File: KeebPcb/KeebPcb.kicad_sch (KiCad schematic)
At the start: 0 parts

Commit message: MCU setup done
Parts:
- added C1: 1uF, symbol Device:C_Small
- added C2, C3, C4: 0.1uF, symbol Device:C_Small
- added C5: 10uF, symbol Device:C_Small
- added C6, C7: 22pF, symbol Device:C_Small
- added R1, R4: 10k, symbol Device:R_Small
- added R2, R3: 22, symbol Device:R_Small
- added SW1: SW_Push, symbol Switch:SW_Push
- added U1: ATmega32U4-A, Package_QFP:TQFP-44_10x10mm_P0.8mm, symbol MCU_Microchip_ATmega:ATmega32U4-A
- added Y1: 16MHz, symbol Device:Crystal_GND24_Small
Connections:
- new net: C1.1, U1.6 (UCAP)
- new net: R3.2, U1.3 (D-)
- new net: R4.2, SW1.2, U1.13 (~{RESET})
- new net: R2.2, U1.4 (D+)
- new net: R1.1, U1.33 (~{HWB}/PE2)
- new net: C6.2, U1.17 (XTAL1), Y1.1
- new net: C7.2, U1.16 (XTAL2), Y1.3
- new net +5V: C2.1, C3.1, C4.1, C5.1, R4.1, U1.14 (VCC), U1.2 (UVCC), U1.24 (AVCC), U1.34 (VCC), U1.44 (AVCC), U1.7 (VBUS)
- new net D+: R2.1
- new net D-: R3.1
- new net GND: C1.2, C2.2, C3.2, C4.2, C5.2, C6.1, C7.1, R1.2, SW1.1, U1.15 (GND), U1.23 (GND), U1.35 (GND), U1.43 (GND), U1.5 (UGND), Y1.2, Y1.4

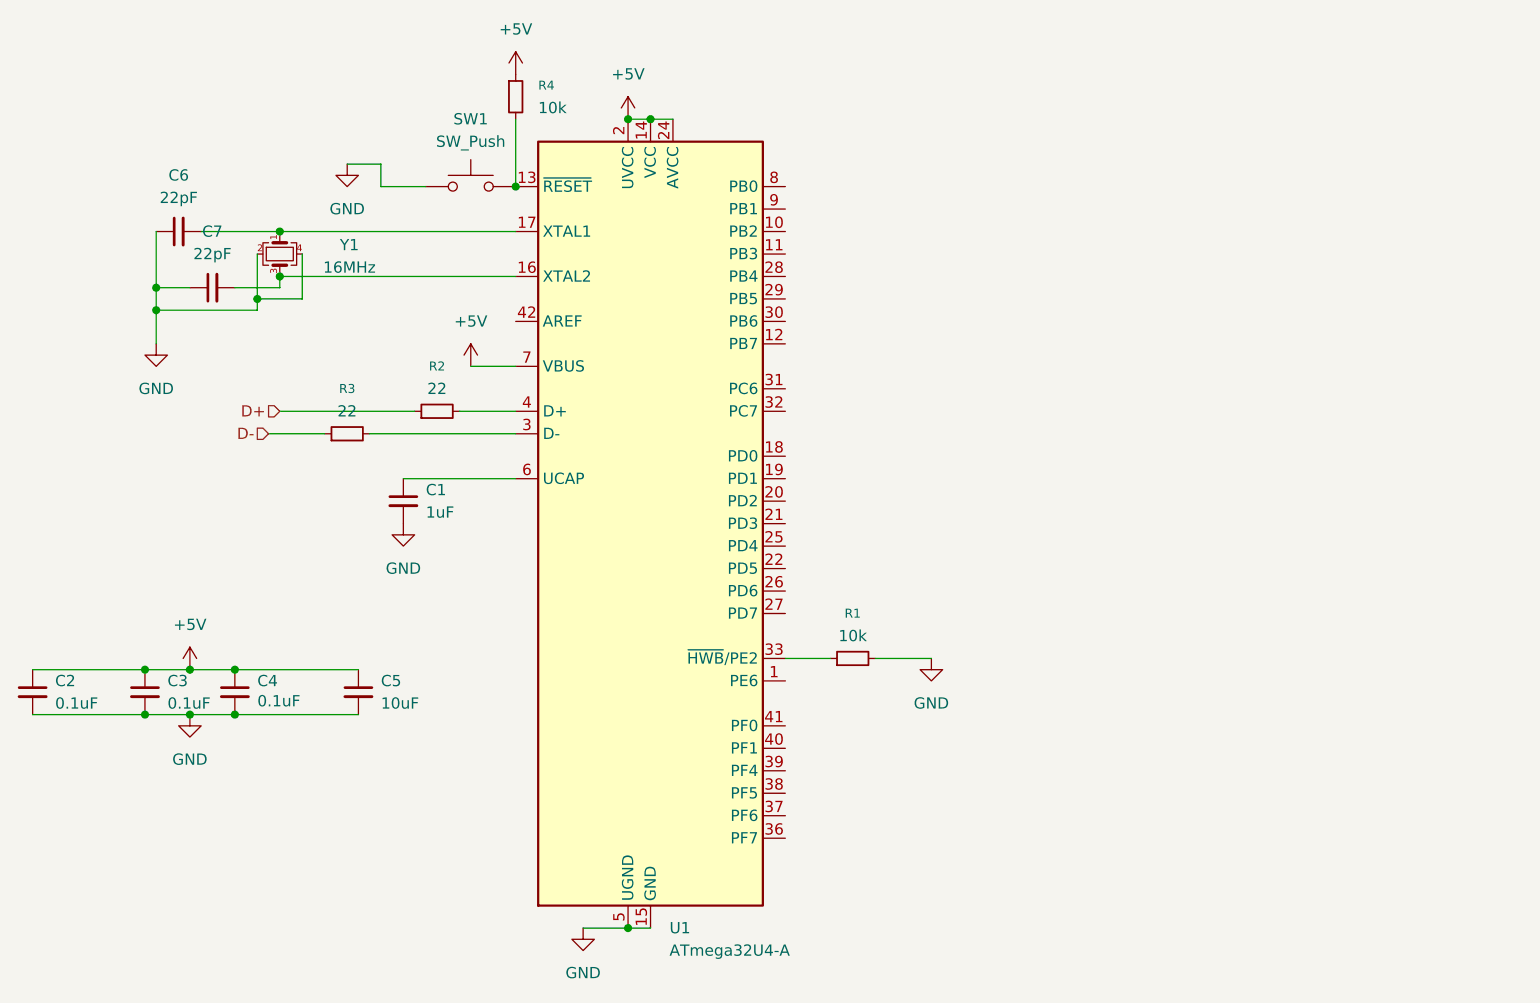
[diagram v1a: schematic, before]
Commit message: Schematic and Footprint bindings done
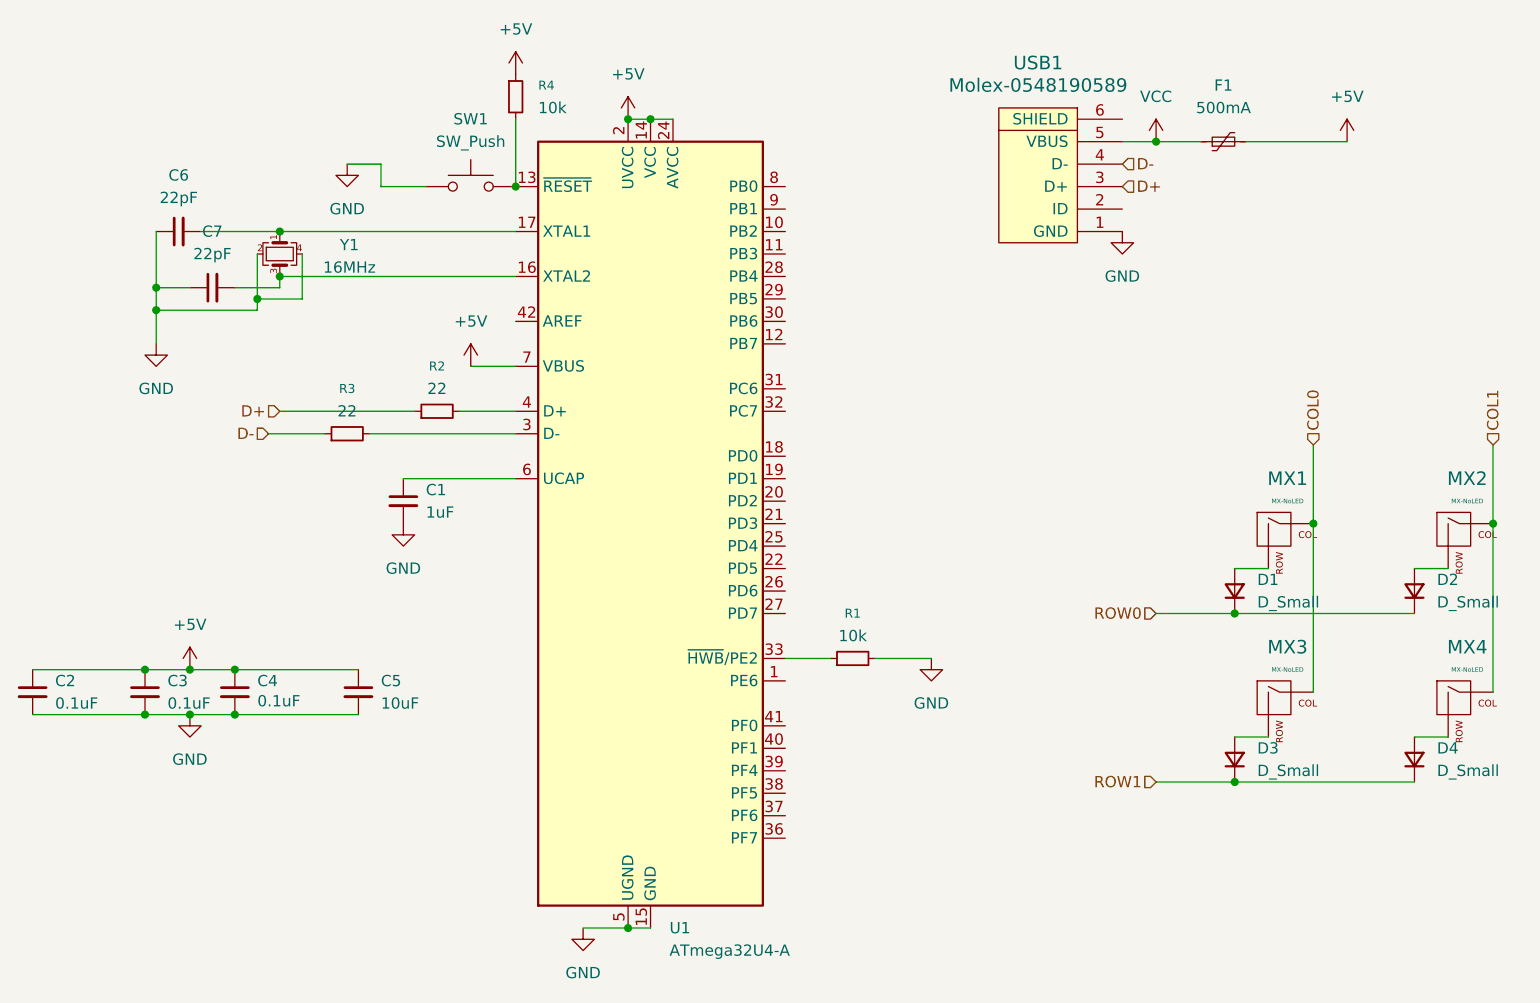
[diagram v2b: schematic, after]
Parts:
- added D1, D2, D3, D4: D_Small, Diode_SMD:D_SOD-123, symbol Device:D_Small
- added F1: 500mA, Fuse:Fuse_1206_3216Metric, symbol Device:Polyfuse_Small
- added MX1, MX2, MX3, MX4: MX-NoLED, MX_Alps_Hybrid:MX-1U-NoLED, symbol MX_Alps_Hybrid:MX-NoLED
- added USB1: Molex-0548190589, random-keyboard-parts:Molex-0548190589, symbol random-keyboard-parts:Molex-0548190589
- C1, C2, C3, C4, C5, C6, C7: footprint (none) -> Capacitor_SMD:C_0805_2012Metric
- R1, R2, R3, R4: footprint (none) -> Resistor_SMD:R_0805_2012Metric
- SW1: footprint (none) -> random-keyboard-parts:SKQG-1155865
- Y1: footprint (none) -> Crystal:Crystal_SMD_SeikoEpson_TSX3225-4Pin_3.2x2.5mm
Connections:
- net +5V: now also F1.2
- net D+: now also USB1.3 (D+)
- net D-: now also USB1.4 (D-)
- net GND: now also USB1.1 (GND)
- new net: D2.2 (A), MX2.2 (ROW)
- new net: D4.2 (A), MX4.2 (ROW)
- new net: D1.2 (A), MX1.2 (ROW)
- new net: D3.2 (A), MX3.2 (ROW)
- new net COL0: MX1.1 (COL), MX3.1 (COL)
- new net COL1: MX2.1 (COL), MX4.1 (COL)
- new net ROW0: D1.1 (K), D2.1 (K)
- new net ROW1: D3.1 (K), D4.1 (K)
- new net VCC: F1.1, USB1.5 (VBUS)

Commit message: Full Design done Pending like changing to USB-C and adding LED
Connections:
- net COL0: now also U1.29 (PB5)
- net COL1: now also U1.28 (PB4)
- net ROW0: now also U1.27 (PD7)
- net ROW1: now also U1.30 (PB6)
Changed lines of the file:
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@@
+		)
+	)
+	(hierarchical_label "COL0"
+		(shape input)
+		(at 163.83 67.31 0)
+		(effects
+			(font
+				(size 1.27 1.27)
+			)
+			(justify left)
 		)
 	)
@@
 		(shape input)
 		(at 201.93 54.61 0)
+		(effects
+			(font
+				(size 1.27 1.27)
+			)
+			(justify left)
+		)
+	)
+	(hierarchical_label "ROW0"
+		(shape input)
+		(at 163.83 102.87 0)
 		(effects
 			(font
@@
 			)
 			(justify right)
+		)
+	)
+	(hierarchical_label "COL1"
+		(shape input)
+		(at 163.83 64.77 0)
+		(effects
+			(font
+				(size 1.27 1.27)
+			)
+			(justify left)
 		)
 	)
@@
 		(effects
 			(font
+				(size 1.27 1.27)
+			)
+			(justify left)
+		)
+	)
+	(hierarchical_label "ROW1"
+		(shape input)
+		(at 163.83 69.85 0)
+		(effects
+			(font
